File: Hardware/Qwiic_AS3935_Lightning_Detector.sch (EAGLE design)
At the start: 31 parts, among them U1 AS3935

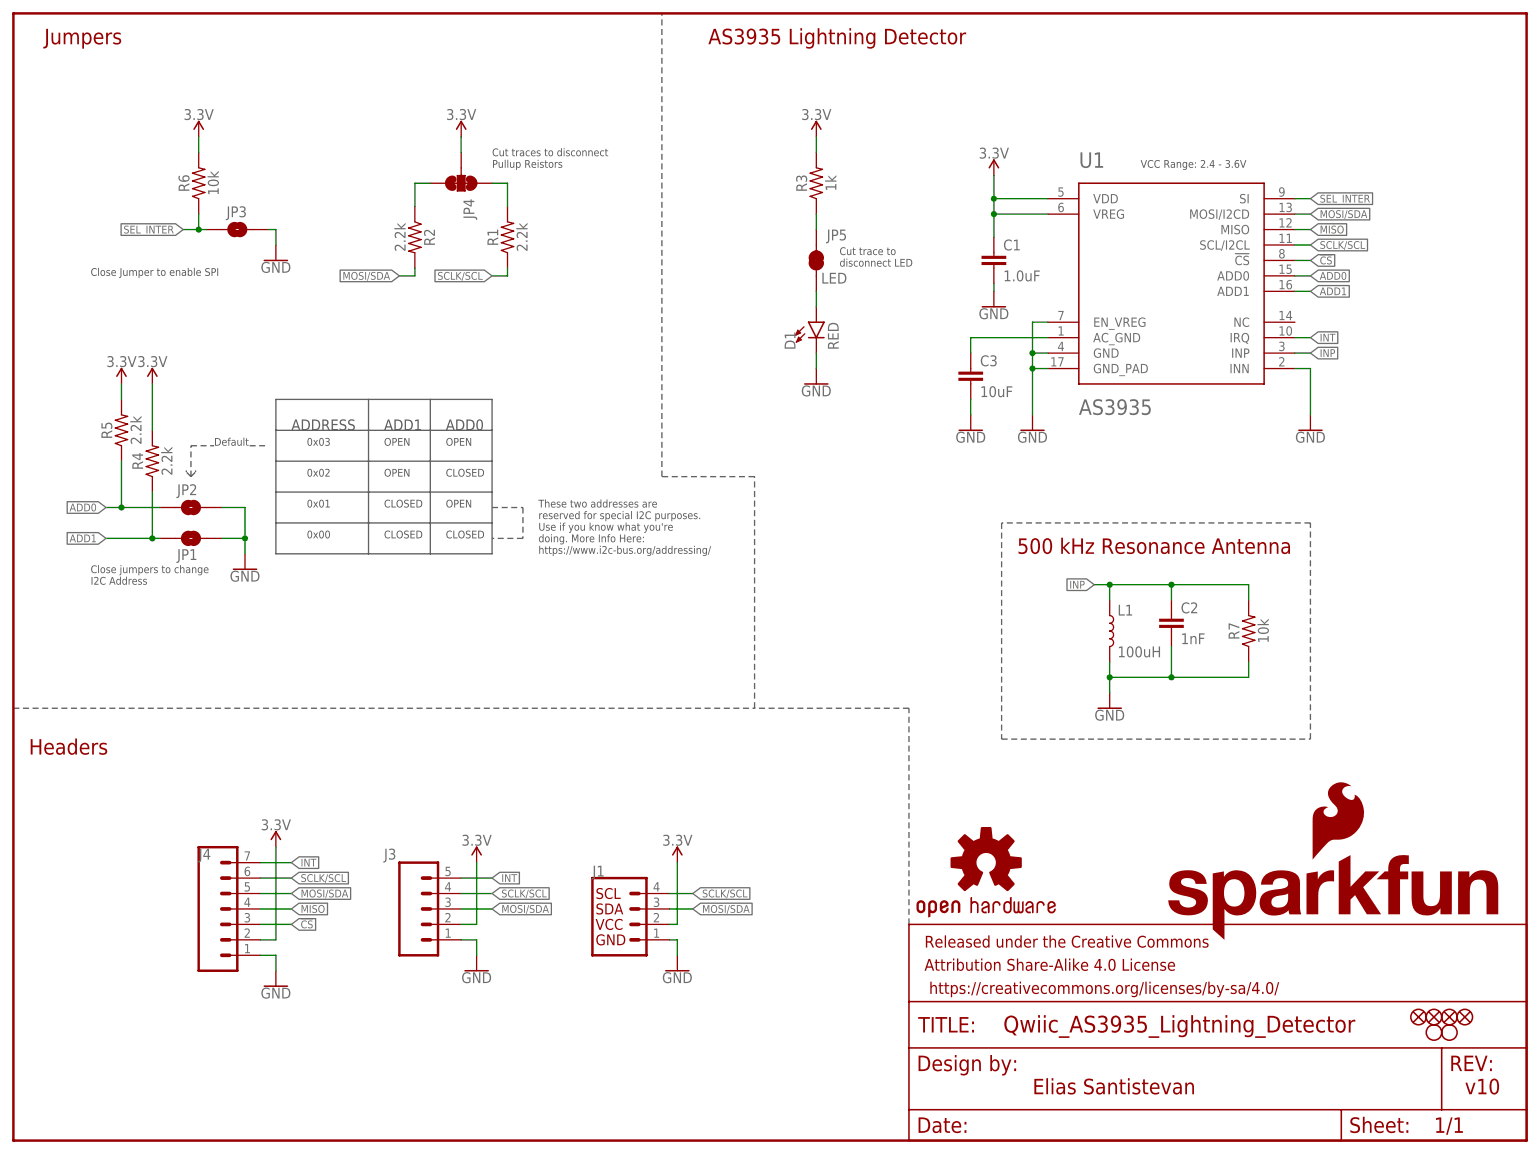
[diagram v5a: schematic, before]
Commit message: List of changes in description from v10 to v11
* Changes three way pull up jumper to disinclude I2C data line - also changes values to 10k
* Removes seperate I2C header and combines I2C and SPI into one header - prevents extraneous trace length on data lines
* Improves layout for better ground pour
* Moves address jumpers and SPI select jumpers
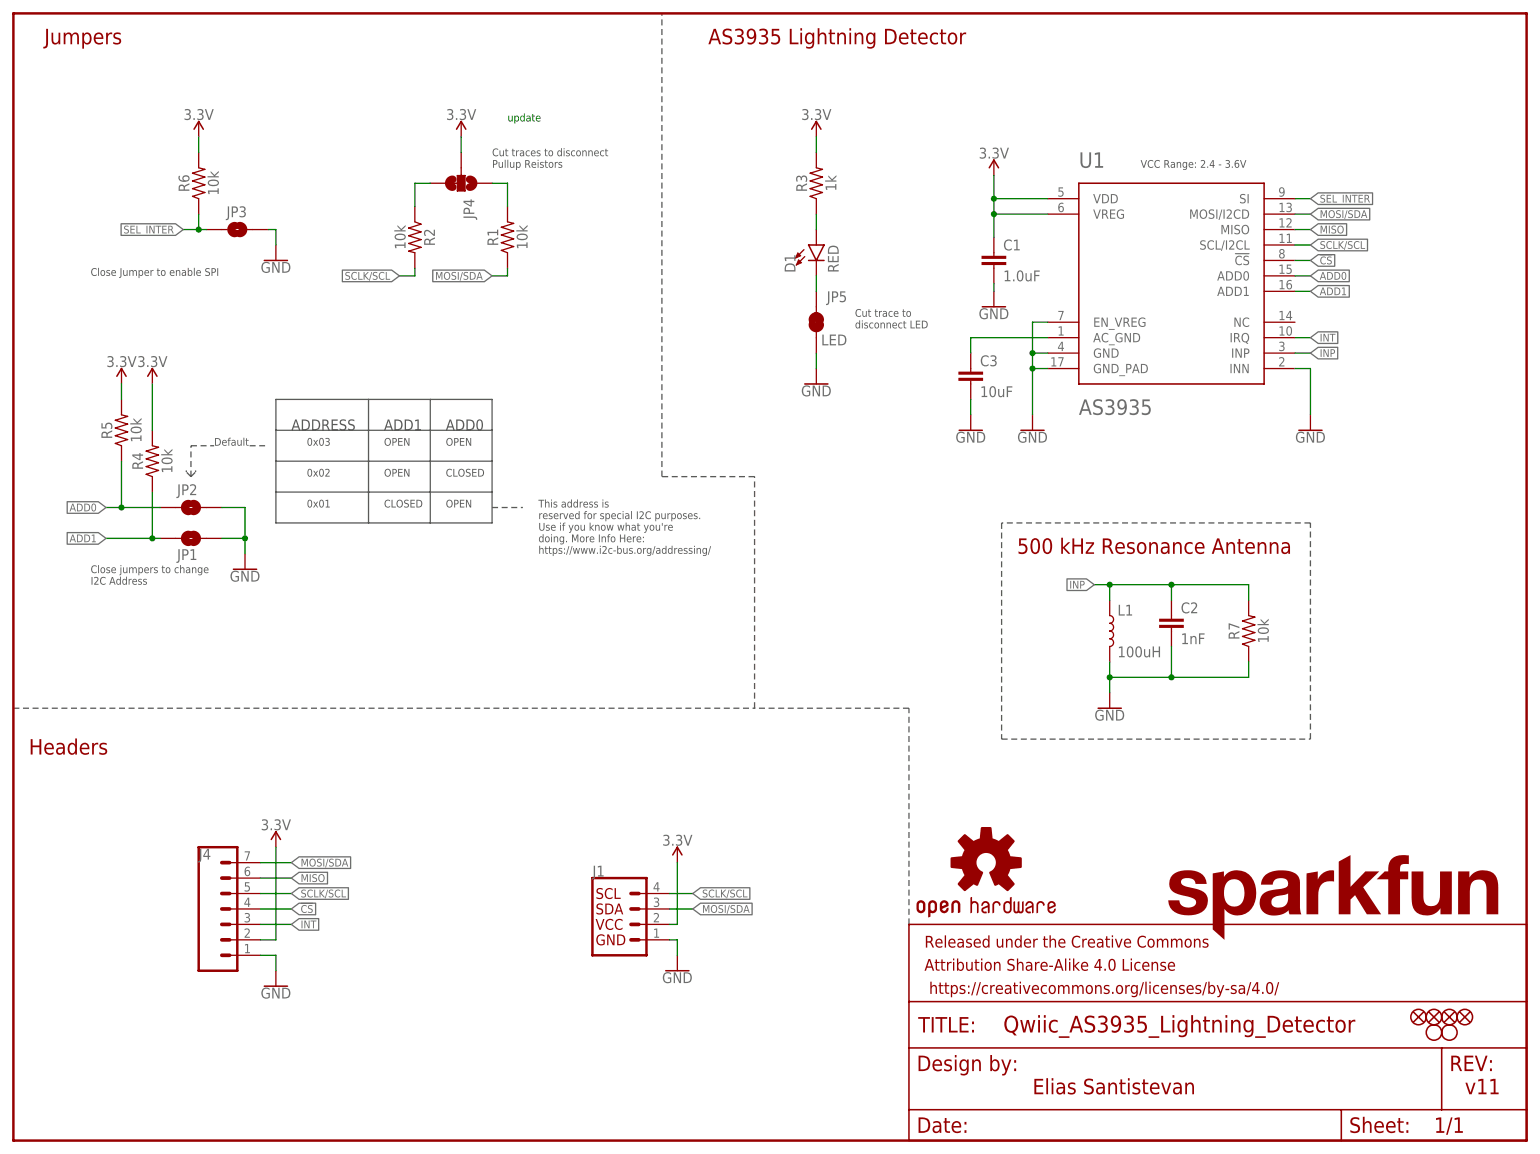
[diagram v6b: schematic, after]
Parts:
- removed J3: (no value), SparkFun-Connectors:CONN_05NO_SILK
- removed LOGO3: SFE_LOGO_FLAME.1_INCH, SparkFun-Aesthetics:SFE_LOGO_FLAME.1_INCH
- JP4: value JUMPER-SMT_3_2-NC_TRACE_SILK -> JUMPER-SMT_3_1-NC_TRACE_SILK; device SparkFun-Jumpers:JUMPER-SMT_3_2-NC_TRACE_SILK -> SparkFun-Jumpers:JUMPER-SMT_3_1-NC_TRACE_SILK
- R1, R2, R4, R5: value 2.2k -> 10k; device SparkFun-Resistors:2.2KOHM-0603-1/10W-1% -> SparkFun-Resistors:10KOHM-0603-1/10W-1%
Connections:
- net !CS: now also J4.4; no longer J4.3
- net 3.3V: no longer J3.2
- net GND: now also JP5.1; no longer D1.C, J3.1
- net INT: now also J4.3; no longer J3.5, J4.7
- net MISO: now also J4.6; no longer J4.4
- net MOSI/SDA: now also J4.7, R1.1; no longer J3.3, J4.5, R2.2
- net N$1: now also D1.A; no longer JP5.2
- net N$5: now also D1.C, JP5.2; no longer D1.A, JP5.1
- net SCLK/SCL: now also J4.5, R2.2; no longer J3.4, J4.6, R1.1
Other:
- note added: "This address is reserved for special I2C purposes. Use if you know what you're doing. More Info Here: https://www.i2c-bus.org/addressing/"
- note added: "update"
- note added: "v11"
- note removed: "0x00"
- note removed: "These two addresses are reserved for special I2C purposes. Use if you know what you're doing. More Info Here: https://www.i2c-bus.org/addressing/"
- note removed: "v10"
- moved on the sheet: D1, JP5

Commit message: Adds "NC" silk, and updates info text in schematic for pullup resistors
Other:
- note added: "R1 is disconnected by default and is not recommended unless there are three or more device on the I2C bus"
- note added: "R2 pullup resistor on the clock is on by default."
- note removed: "Cut traces to disconnect Pullup Reistors"
- note removed: "update"
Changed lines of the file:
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@@
 <text x="165.1" y="96.52" size="2.54" layer="94" font="vector">500 kHz Resonance Antenna</text>
 <text x="12.7" y="142.24" size="1.27" layer="97" font="vector">Close Jumper to enable SPI</text>
-<text x="78.74" y="160.02" size="1.27" layer="97" font="vector">Cut traces to disconnect
-Pullup Reistors</text>
+<text x="78.74" y="160.02" size="1.27" layer="97" font="vector">R1 is disconnected by default
+and is not recommended unless
+there are three or more device
+on the I2C bus</text>
 <text x="12.7" y="91.44" size="1.27" layer="97" font="vector">Close jumpers to change
 I2C Address</text>
@@
 <wire x1="29.21" y1="109.22" x2="28.448" y2="109.982" width="0.2032" layer="97" style="shortdash"/>
 <wire x1="28.448" y1="109.982" x2="28.448" y2="110.236" width="0.2032" layer="97" style="shortdash"/>
-<text x="81.28" y="167.64" size="1.27" layer="91" font="vector">update</text>
+<text x="50.8" y="160.02" size="1.27" layer="97" font="vector">R2 pullup resistor
+on the clock is on
+by default. </text>
 </plain>
 <instances>

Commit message: Adds flame to underside (hur hur), adds additional path in bottom pour. changes jumper names to address rather than jumper
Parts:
- added LOGO3: SFE_LOGO_FLAME.2_INCH, SparkFun-Aesthetics:SFE_LOGO_FLAME.2_INCH
- renumbered JP1 to ADD1, JP2 to ADD0
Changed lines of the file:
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@@
 <part name="GND1" library="SparkFun-PowerSymbols" deviceset="GND" device=""/>
 <part name="C1" library="SparkFun-Capacitors" deviceset="1.0UF" device="-0603-16V-10%" value="1.0uF"/>
-<part name="JP2" library="SparkFun-Jumpers" deviceset="JUMPER-SMT_2_NO" device="_SILK"/>
+<part name="ADD0" library="SparkFun-Jumpers" deviceset="JUMPER-SMT_2_NO" device="_SILK"/>
 <part name="R5" library="SparkFun-Resistors" deviceset="10KOHM" device="-0603-1/10W-1%" value="10k"/>
 <part name="GND2" library="SparkFun-PowerSymbols" deviceset="GND" device=""/>
 <part name="SUPPLY3" library="SparkFun-PowerSymbols" deviceset="3.3V" device=""/>
-<part name="JP1" library="SparkFun-Jumpers" deviceset="JUMPER-SMT_2_NO" device="_SILK"/>
+<part name="ADD1" library="SparkFun-Jumpers" deviceset="JUMPER-SMT_2_NO" device="_SILK"/>
 <part name="R4" library="SparkFun-Resistors" deviceset="10KOHM" device="-0603-1/10W-1%" value="10k"/>
 <part name="SUPPLY4" library="SparkFun-PowerSymbols" deviceset="3.3V" device=""/>
@@
 <part name="H2" library="SparkFun-Hardware" deviceset="STAND-OFF" device="TIGHT"/>
 <part name="JP5" library="SparkFun-Jumpers" deviceset="JUMPER-SMT_2_NC_TRACE" device="_SILK" value="LED"/>
+<part name="LOGO3" library="SparkFun-Aesthetics" deviceset="SFE_LOGO_FLAME" device=".2_INCH"/>
 </parts>
 <sheets>
@@
 <attribute name="VALUE" x="162.814" y="141.351" size="1.778" layer="96" font="vector"/>
 </instance>
-<instance part="JP2" gate="G$1" x="29.21" y="104.14" smashed="yes">
+<instance part="ADD0" gate="G$1" x="29.21" y="104.14" smashed="yes">
 <attribute name="NAME" x="26.924" y="106.172" size="1.778" layer="95" font="vector"/>
 </instance>
@@
 <attribute name="VALUE" x="73.66" y="167.894" size="1.778" layer="96" align="bottom-center"/>
 </instance>
-<instance part="JP1" gate="G$1" x="29.21" y="99.06" smashed="yes">
+<instance part="ADD1" gate="G$1" x="29.21" y="99.06" smashed="yes">
 <attribute name="NAME" x="26.924" y="95.504" size="1.778" layer="95" font="vector"/>
 </instance>
@@
 <attribute name="VALUE" x="137.16" y="130.81" size="1.778" layer="96" font="vector" rot="R180" align="top-left"/>
 </instance>
+<instance part="LOGO3" gate="G$1" x="223.52" y="45.72" smashed="yes"/>
 </instances>
 <busses>
@@
 </segment>
 <segment>
-<pinref part="JP2" gate="G$1" pin="2"/>
+<pinref part="ADD0" gate="G$1" pin="2"/>
 <wire x1="34.29" y1="104.14" x2="38.1" y2="104.14" width="0.1524" layer="91"/>
 <wire x1="38.1" y1="104.14" x2="38.1" y2="99.06" width="0.1524" layer="91"/>
-<pinref part="JP1" gate="G$1" pin="2"/>
+<pinref part="ADD1" gate="G$1" pin="2"/>
 <wire x1="38.1" y1="99.06" x2="38.1" y2="96.52" width="0.1524" layer="91"/>
 <wire x1="34.29" y1="99.06" x2="38.1" y2="99.06" width="0.1524" layer="91"/>
@@
 <net name="ADD0" class="0">
 <segment>
-<pinref part="JP2" gate="G$1" pin="1"/>
+<pinref part="ADD0" gate="G$1" pin="1"/>
 <wire x1="24.13" y1="104.14" x2="17.78" y2="104.14" width="0.1524" layer="91"/>
 <label x="15.24" y="104.14" size="1.27" layer="95" font="vector" rot="R180" xref="yes"/>
@@
 <net name="ADD1" class="0">
 <segment>
-<pinref part="JP1" gate="G$1" pin="1"/>
+<pinref part="ADD1" gate="G$1" pin="1"/>
 <wire x1="15.24" y1="99.06" x2="22.86" y2="99.06" width="0.1524" layer="91"/>
 <label x="15.24" y="99.06" size="1.27" layer="95" font="vector" rot="R180" xref="yes"/>
